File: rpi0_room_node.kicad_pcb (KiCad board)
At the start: 2 copper layers, 65 x 30 mm, 28 parts, among them J1 Raspberry Pi, J2 Conn_01x03, Q1 PDTC123Y, U1 AP2210K-3.3, U2 TSOP382xx, U3 RFM69HCW

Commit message: Layouting
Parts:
- removed C5: C, Capacitor_SMD:C_0805_2012Metric_Pad1.15x1.40mm_HandSolder
- added AE1: Antenna_Shield, Connector_Coaxial:SMA_Amphenol_132289_EdgeMount, F.Cu at (158.0, 110.0)
- added J3: Conn_01x03, Connector_PinHeader_2.54mm:PinHeader_1x03_P2.54mm_Vertical, F.Cu at (125.0, 105.0)
- R6, R7, R8: moved to B.Cu
- moved D1 69.7 mm to (158.0, 118.0), turned to 180 degrees
- moved R6 60.0 mm to (145.0, 105.0), turned to 90 degrees
- moved R7 58.2 mm to (143.0, 105.0), turned to 90 degrees
- moved R8 54.6 mm to (141.0, 105.0), turned to 90 degrees
- moved C1 31.8 mm to (129.0, 105.0), turned to 270 degrees
- moved U1 27.8 mm to (132.1, 105.0), turned to 270 degrees
- moved R4 24.8 mm to (111.0, 105.0)
- moved C2 24.1 mm to (135.0, 105.0), turned to 90 degrees
- moved R3 23.3 mm to (107.0, 105.0)
- moved D4 22.0 mm to (113.0, 105.0)
- moved D3 20.6 mm to (109.0, 105.0)
- moved C4 19.3 mm to (135.0, 109.0), turned to 270 degrees
- moved R5 18.9 mm to (115.0, 105.0)
- moved D5 15.6 mm to (117.0, 105.0)
- moved R2 10.9 mm to (104.5, 115.0), turned to 90 degrees
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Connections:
- net /RFM_DIO5 renamed Net-(U3-Pad7)
- J1 pad 10: Net-(J1-Pad10) -> /RXD
- J1 pad 13: Net-(J1-Pad13) -> /LED3
- J1 pad 15: Net-(J1-Pad15) -> /RFM_RST
- J1 pad 18: Net-(J1-Pad18) -> /RFM_DIO1
- J1 pad 22: Net-(J1-Pad22) -> /RFM_DIO0
- J1 pad 29: Net-(J1-Pad29) -> /LEDR
- J1 pad 3: Net-(J1-Pad3) -> /LED1
- J1 pad 31: Net-(J1-Pad31) -> /LEDG
- J1 pad 32: Net-(J1-Pad32) -> /LEDB
- J1 pad 5: Net-(J1-Pad5) -> /LED2
- J1 pad 8: Net-(J1-Pad8) -> /TXD
- R3 pad 1: Net-(R3-Pad1) -> /LED1
- R4 pad 1: Net-(R4-Pad1) -> /LED2
- R5 pad 1: Net-(R5-Pad1) -> /LED3
- R6 pad 1: Net-(R6-Pad1) -> /LEDB
- R7 pad 1: Net-(R7-Pad1) -> /LEDG
- R8 pad 1: Net-(R8-Pad1) -> /LEDR
- U3 pad 15: Net-(U3-Pad15) -> /RFM_DIO1

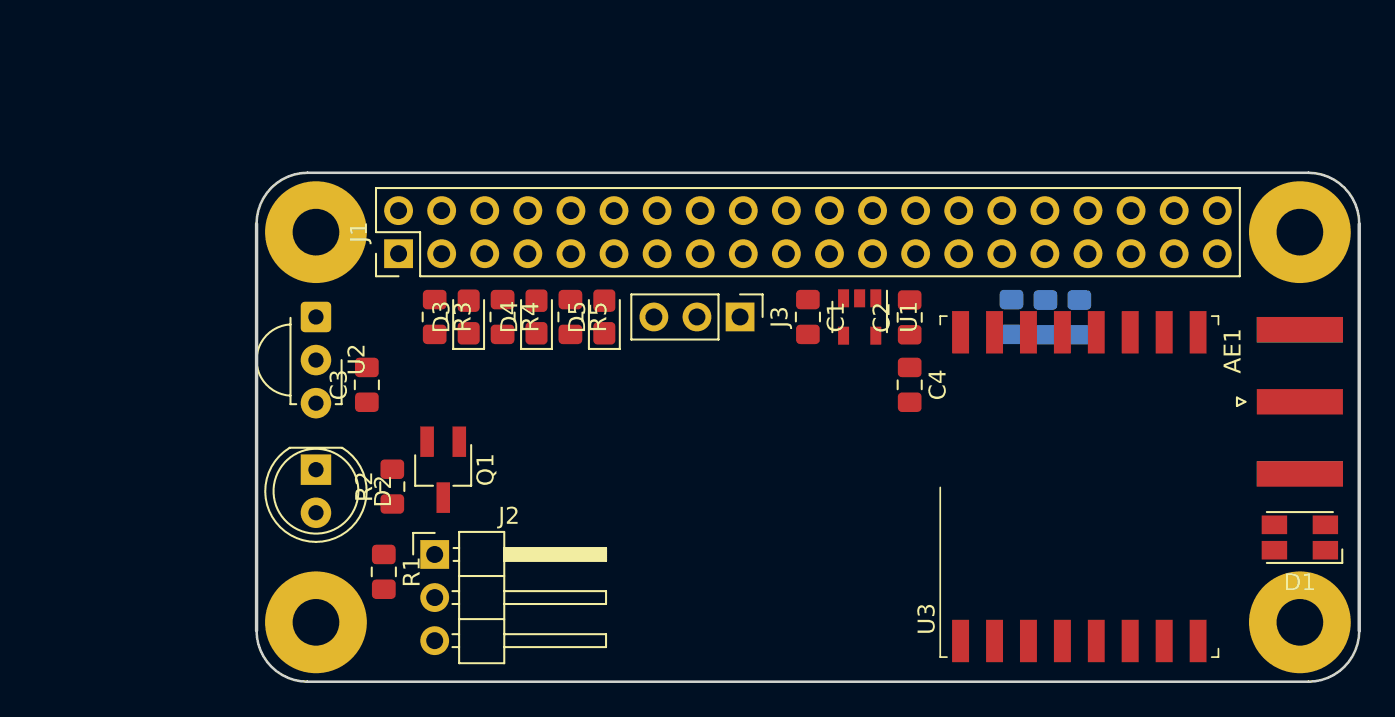
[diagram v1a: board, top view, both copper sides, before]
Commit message: Add u.fl and second onewire header
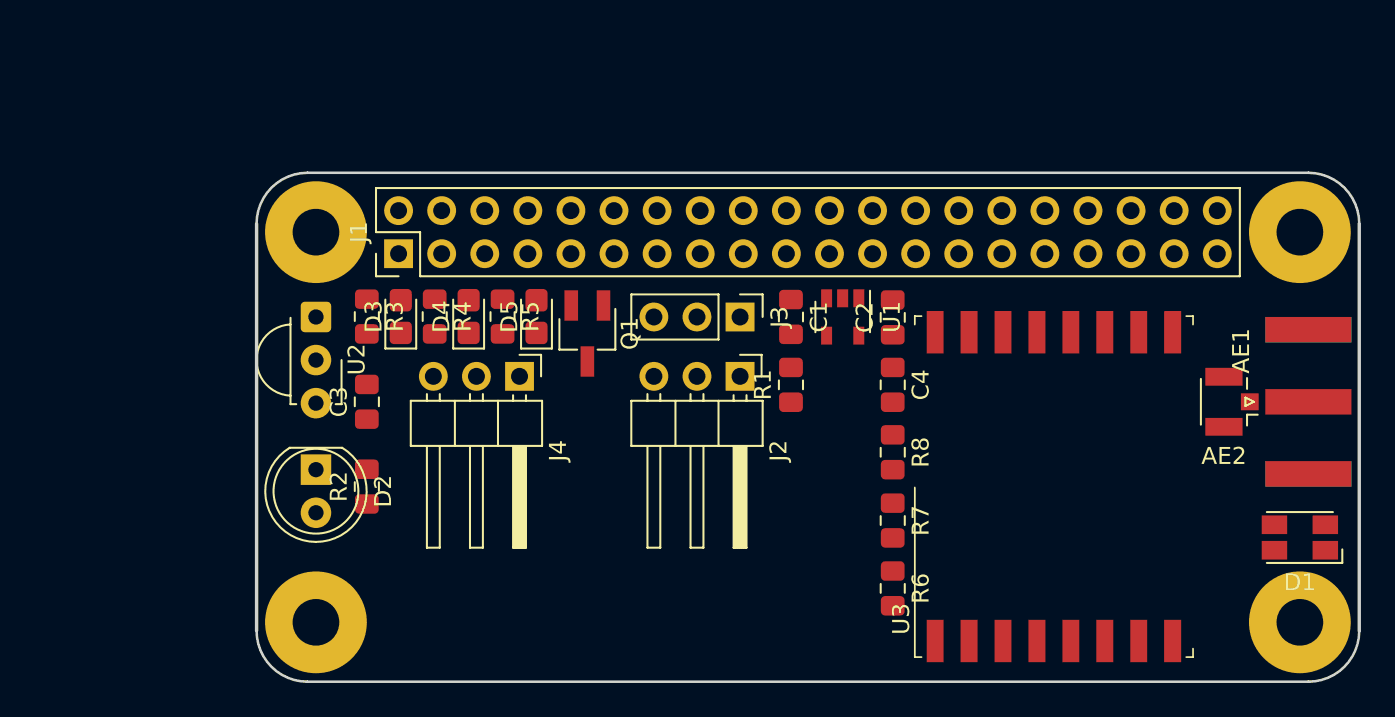
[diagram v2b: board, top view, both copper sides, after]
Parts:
- added AE2: U.FL, Connector_Coaxial:U.FL_Hirose_U.FL-R-SMT-1_Vertical, F.Cu at (154.0, 110.0)
- added J4: Conn_01x03, Connector_PinHeader_2.54mm:PinHeader_1x03_P2.54mm_Horizontal, F.Cu at (112.0, 108.5)
- AE1: value Antenna_Shield -> SMA
- R6, R7, R8: moved to F.Cu
- moved R1 26.4 mm to (128.0, 109.0), turned to 90 degrees
- moved J2 20.8 mm to (125.0, 108.5), turned to 270 degrees
- moved R6 19.4 mm to (134.0, 121.0), turned to 270 degrees
- moved R7 15.0 mm to (134.0, 117.0), turned to 270 degrees
- moved Q1 11.7 mm to (116.0, 106.0)
- moved R8 10.6 mm to (134.0, 113.0), turned to 270 degrees
- moved D3 4.00 mm to (105.0, 105.0)
- moved D4 4.00 mm to (109.0, 105.0)
- moved D5 4.00 mm to (113.0, 105.0)
- moved R3 4.00 mm to (103.0, 105.0)
- moved R4 4.00 mm to (107.0, 105.0)
- moved R5 4.00 mm to (111.0, 105.0)
- moved R2 1.50 mm to (103.0, 115.0)
- moved U3 1.50 mm to (143.5, 115.0)
- moved C1 1.00 mm to (128.0, 105.0)
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
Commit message: Add prototyping area
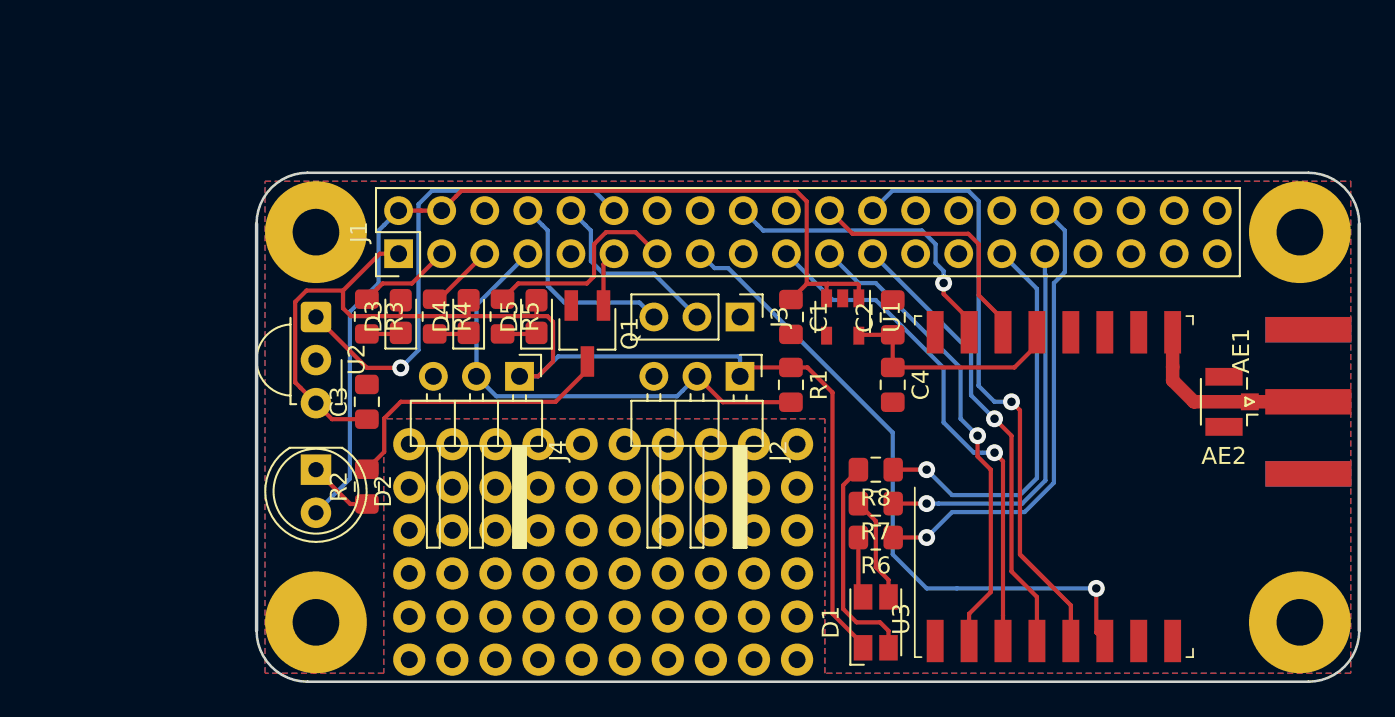
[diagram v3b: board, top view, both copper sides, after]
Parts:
- added REF**: protoarea, protoarea:protoarea, F.Cu at (105.5, 112.5)
- moved D1 25.5 mm to (133.0, 123.0), turned to 90 degrees
- moved R6 3.16 mm to (133.0, 118.0), turned to 180 degrees
- moved R8 1.43 mm to (133.0, 114.0), turned to 180 degrees
- moved R7 1.41 mm to (133.0, 116.0), turned to 180 degrees
- turned R1 to 270 degrees
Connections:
- net Net-(AE1-Pad1) renamed /ANT
- U3 pad 5: /CS0 -> /CE0
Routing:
- net +3V3: track 0.00 -> 75.1 mm
- net +5V: track 0.00 -> 55.6 mm
- net /RFM_RST: track 0.00 -> 39.0 mm, vias 0 -> 1
- net /CE0: track 0.00 -> 38.6 mm, vias 0 -> 1
- net /MOSI: track 0.00 -> 30.3 mm, vias 0 -> 1
- net /IRRX: track 0.00 -> 28.7 mm, vias 0 -> 1
- net /ONEWIRE: track 0.00 -> 28.6 mm
- net /MISO: track 0.00 -> 27.9 mm, vias 0 -> 1
- net /LEDB: track 0.00 -> 27.6 mm, vias 0 -> 1
- net /SCLK: track 0.00 -> 26.8 mm, vias 0 -> 1
- net /LEDR: track 0.00 -> 23.6 mm, vias 0 -> 1
- net /LEDG: track 0.00 -> 22.9 mm, vias 0 -> 1
- net /RFM_DIO1: track 0.00 -> 18.2 mm, vias 0 -> 1
- net Net-(Q1-Pad3): track 0.00 -> 17.1 mm
- net /RFM_DIO0: track 0.00 -> 15.4 mm
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- added copper zone on B.Cu, net GND
- added copper zone on F.Cu, net GND
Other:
- net class ANT added: clearance 0.5, trace_width 0.8, via_dia 0.8, via_drill 0.4
- net class Default: via_dia 0.8 -> 1; via_drill 0.4 -> 0.5

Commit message: Clean up silkscreen
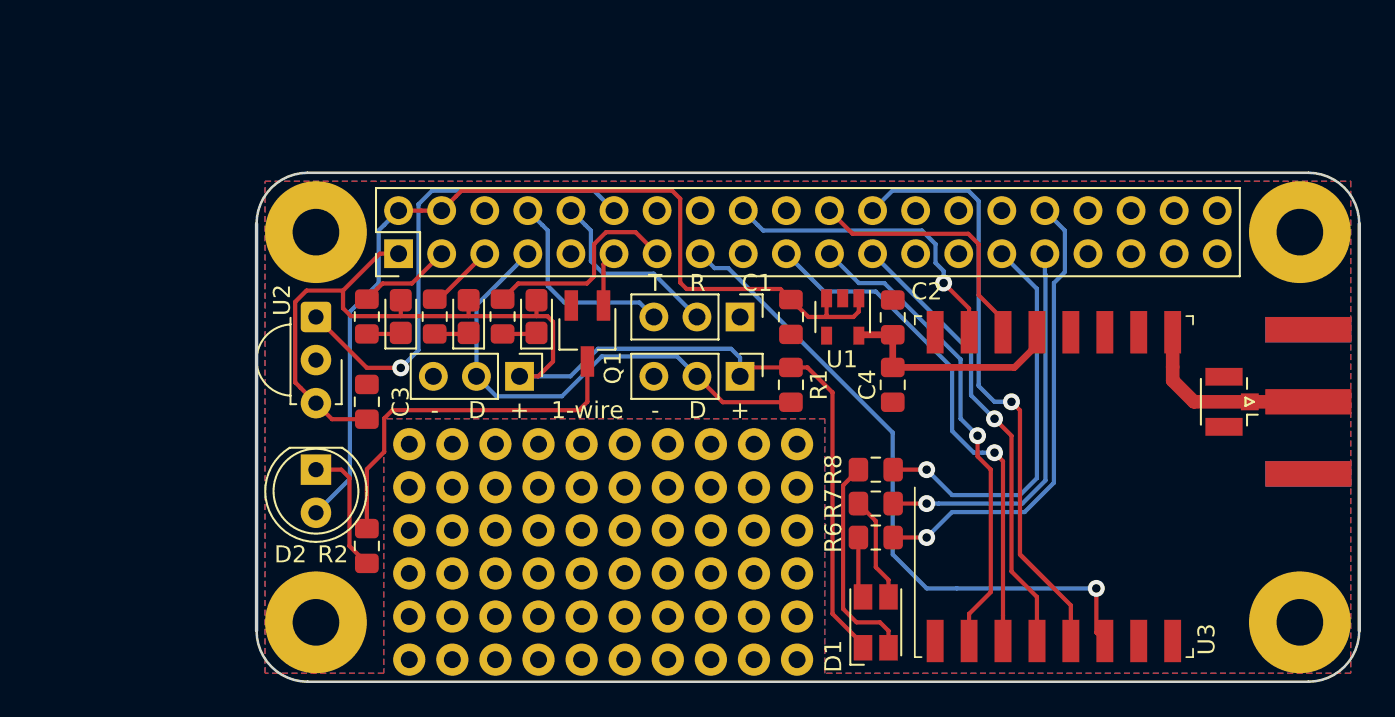
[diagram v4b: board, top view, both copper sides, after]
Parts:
- J2, J4: footprint Connector_PinHeader_2.54mm:PinHeader_1x03_P2.54mm_Horizontal -> Connector_PinHeader_2.54mm:PinHeader_1x03_P2.54mm_Vertical
- moved R2 3.50 mm to (103.0, 118.5)
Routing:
- net Net-(Q1-Pad3): track 17.1 -> 21.7 mm
- net Net-(D2-Pad1): track 3.84 -> 7.65 mm
- net /ONEWIRE: track 28.6 -> 29.6 mm
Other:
- board text added: "+"
- board text added: "-"
- board text added: "1-wire"
- board text added: "D"
- board text added: "R"
- board text added: "T"

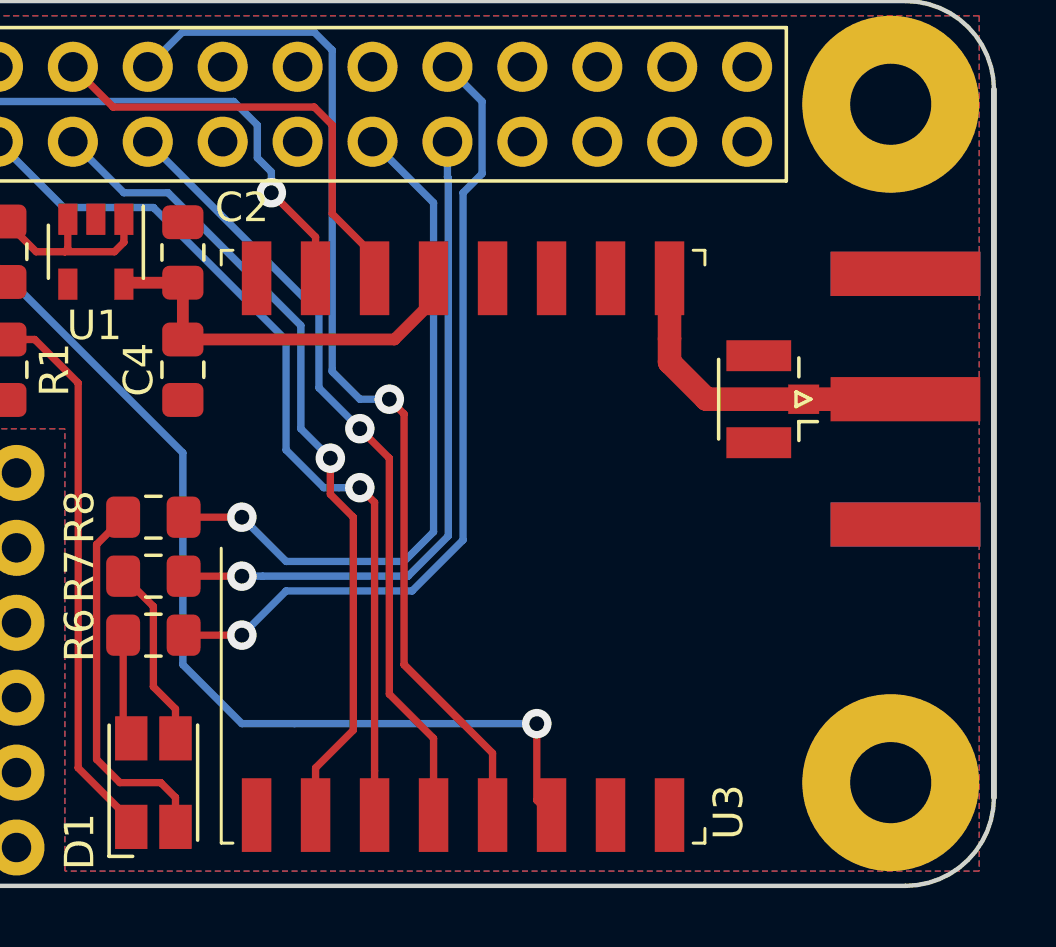
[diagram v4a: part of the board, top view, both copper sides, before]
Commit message: Silkscreen improvements
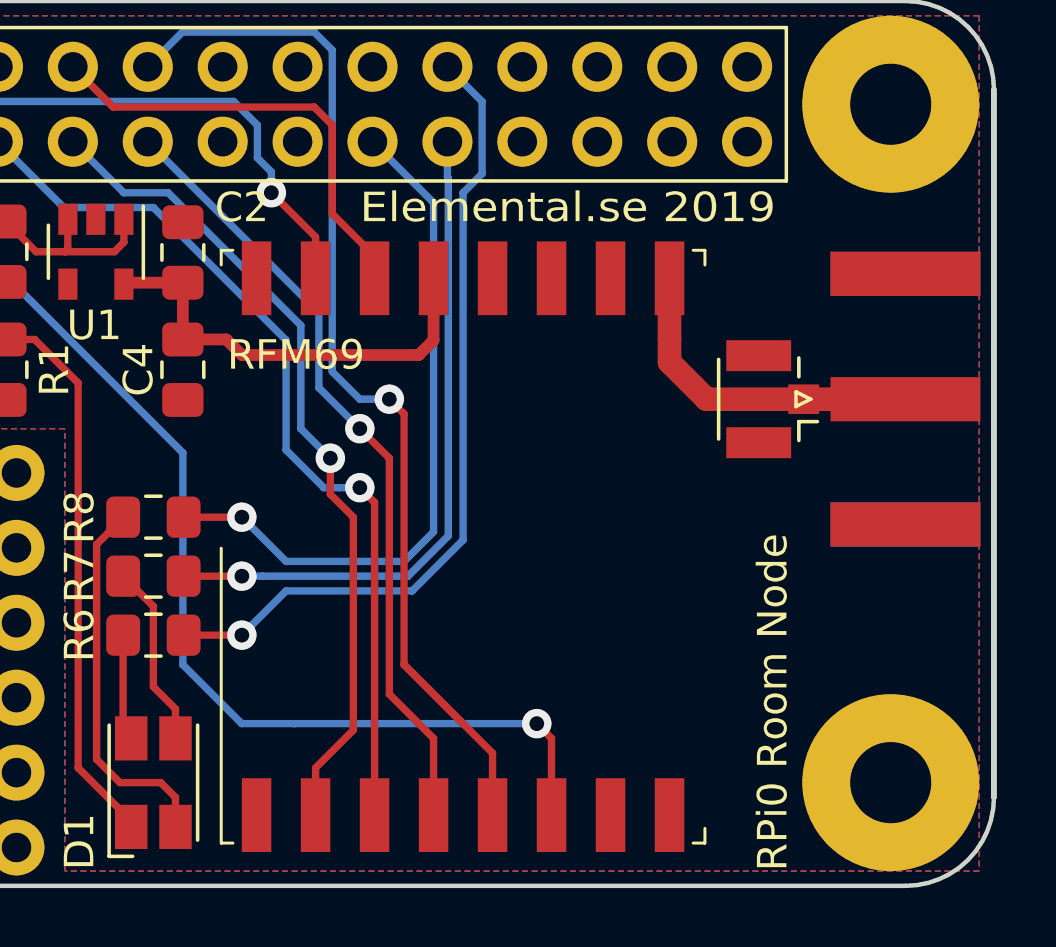
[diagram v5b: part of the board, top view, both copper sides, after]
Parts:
- added G***: LOGO, elemental:elemental-4mm-mask, F.Cu at (158.0, 117.5)
- added G***: LOGO, elemental:elemental-25.4mm, B.Cu at (145.0, 115.5)
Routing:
- net VDDA: track 13.7 -> 15.7 mm
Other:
- board text added: "1wire"
- board text added: "3.3V"
- board text added: "Elemental.se 2019"
- board text added: "GND"
- board text added: "IR RX"
- board text added: "IR TX"
- board text added: "RFM69"
- board text added: "RPi0 Room Node"
- board text added: "SMA"
- board text added: "serial"
